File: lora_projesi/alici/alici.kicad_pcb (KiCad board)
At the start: 4 copper layers, 88 x 102 mm, 127 parts, among them J1 USB-C, J2 SMA, J3 RJ45, J4 u.FL (ANA ANTEN), J5 12 V GIRIS, J6 LAMBA, J7 MICRO-SIM, J8 u.FL (YARDIMCI ANTEN, ISTEGE 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, K1 SRD-12VDC-SL-A, Q1 AO3401A, Q2 MMBT2222A, Q3 MMBT2222A, Q4 MMBT2222A, SW1 DUGME, U1 ESP32-S3-WROOM-1-N4, U10 SIM7600SA, U11 AP2112K-3.3, U12 ESDA6V1-5SC6, U4 RFM95W-915S2, U5 TPS62933DRLR, U6 TPS62933DRLR, U7 USBLC6-2SC6, U8 TXB0104PW, U9 W5500, Y1 25 MHz

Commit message: Alici: uretim dosyalari (Gerber, delik, BOM, yerlestirme, PDF)
Co-Authored-By: Claude Sonnet 5.5 <noreply@anthropic.com>
Claude-Session: https://claude.ai/code/session_01Q71gHQtKJ86ZE2CtYTYSwP
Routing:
- net GND: track 232.1 -> 237.4 mm, vias 232 -> 234
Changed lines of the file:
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@@
   (segment (start 35.277707 20.227637) (end 36.177707 20.227637) (width 0.25) (layer "F.Cu") (net 93))
   (segment (start 10.8 91.12) (end 10.8 89.72) (width 0.25) (layer "F.Cu") (net 93))
+  (segment (start 31.15 27.65) (end 31.25 27.75) (width 0.25) (layer "F.Cu") (net 93))
   (segment (start 74.75 90.26) (end 75.65 90.26) (width 0.25) (layer "F.Cu") (net 93))
   (segment (start 37.5 31.9) (end 37.5 32.799999) (width 0.25) (layer "F.Cu") (net 93))
+  (segment (start 31.25 27.75) (end 31.75 27.75) (width 0.25) (layer "F.Cu") (net 93))
   (segment (start 54.75 66.1625) (end 54.75 65.0625) (width 0.25) (layer "F.Cu") (net 93))
+  (segment (start 31.75 27.75) (end 31.8 27.8) (width 0.25) (layer "F.Cu") (net 93))
   (segment (start 51.182401 11.420149) (end 52.082401 11.420149) (width 0.25) (layer "F.Cu") (net 93))
   (segment (start 43.1 37.5) (end 44 37.5) (width 0.25) (layer "F.Cu") (net 93))
@@
   (segment (start 12.9 49.5) (end 13.8 49.5) (width 0.25) (layer "F.Cu") (net 93))
   (segment (start 40.446899 4.070346) (end 41.346899 4.070346) (width 0.25) (layer "F.Cu") (net 93))
+  (segment (start 32.2 28.2) (end 32.2 28.4) (width 0.25) (layer "F.Cu") (net 93))
   (segment (start 50.41465 6.192358) (end 51.051046 6.828754) (width 0.25) (layer "F.Cu") (net 93))
   (segment (start 62.475 11) (end 63.111396 11.636396) (width 0.25) (layer "F.Cu") (net 93))
@@
   (segment (start 46.2125 87) (end 46.848896 87.636396) (width 0.25) (layer "F.Cu") (net 93))
   (segment (start 55.172717 71.925954) (end 56.072717 71.925954) (width 0.25) (layer "F.Cu") (net 93))
+  (segment (start 31.9 27.85) (end 31.9 27.9) (width 0.25) (layer "F.Cu") (net 93))
   (segment (start 37.5 62.1) (end 37.5 61.2) (width 0.25) (layer "F.Cu") (net 93))
   (segment (start 17.2 91.12) (end 19 91.12) (width 0.25) (layer "F.Cu") (net 93))
@@
   (segment (start 44.41465 70.192358) (end 45.31465 70.192358) (width 0.25) (layer "F.Cu") (net 93))
   (segment (start 67.343346 49.686625) (end 68.243346 49.686625) (width 0.25) (layer "F.Cu") (net 93))
+  (segment (start 31.8 27.8) (end 31.85 27.8) (width 0.25) (layer "F.Cu") (net 93))
   (segment (start 21.5 31.9) (end 20.863603 32.536396) (width 0.25) (layer "F.Cu") (net 93))
   (segment (start 58.25 4.5) (end 58.25 5.4) (width 0.25) (layer "F.Cu") (net 93))
   (segment (start 9.581158 35.759225) (end 10.481158 35.759225) (width 0.25) (layer "F.Cu") (net 93))
   (segment (start 42.2125 87) (end 42.848896 87.636396) (width 0.25) (layer "F.Cu") (net 93))
+  (segment (start 31.85 27.8) (end 31.9 27.85) (width 0.25) (layer "F.Cu") (net 93))
   (segment (start 32.85 87.9) (end 33.486396 88.536396) (width 0.25) (layer "F.Cu") (net 93))
   (segment (start 25.1375 28.95) (end 21.441981 30.480733) (width 0.25) (layer "F.Cu") (net 93))
@@
   (segment (start 80.098289 75.215095) (end 80.998289 75.215095) (width 0.25) (layer "F.Cu") (net 93))
   (segment (start 44.090413 64.908678) (end 44.726809 65.545074) (width 0.25) (layer "F.Cu") (net 93))
+  (segment (start 31.9 27.9) (end 32.2 28.2) (width 0.25) (layer "F.Cu") (net 93))
   (segment (start 24.2 28.8) (end 24.25 28.85) (width 0.25) (layer "F.Cu") (net 93))
   (segment (start 67.5 82.54) (end 66.863603 83.176396) (width 0.25) (layer "F.Cu") (net 93))
@@
   (segment (start 12.9 49.5) (end 12 49.5) (width 0.25) (layer "F.Cu") (net 93))
   (segment (start 55.122479 84.448638) (end 55.758875 85.085034) (width 0.25) (layer "F.Cu") (net 93))
+  (segment (start 32.2 28.4) (end 32.65 28.85) (width 0.25) (layer "F.Cu") (net 93))
   (segment (start 36.250064 4.42492) (end 37.150064 4.42492) (width 0.25) (layer "F.Cu") (net 93))
   (segment (start 24.05 28.65) (end 24.1 28.7) (width 0.25) (layer "F.Cu") (net 93))
@@
   (segment (start 35.277707 20.227637) (end 35.914103 20.864033) (width 0.25) (layer "F.Cu") (net 93))
   (segment (start 66.738361 40.358364) (end 67.638361 40.358364) (width 0.25) (layer "F.Cu") (net 93))
+  (segment (start 30.8625 27.65) (end 31.15 27.65) (width 0.25) (layer "F.Cu") (net 93))
   (segment (start 37.5 62.1) (end 38.18883 63.762983) (width 0.25) (layer "F.Cu") (net 93))
   (segment (start 18.5 31.9) (end 18.5 32.799999) (width 0.25) (layer "F.Cu") (net 93))
@@
   (via (at 10.8 89.72) (size 0.5) (drill 0.25) (layers "F.Cu" "B.Cu") (net 93))
   (via (at 34.772645 61.880584) (size 0.5) (drill 0.25) (layers "F.Cu" "B.Cu") (net 93))
+  (via (at 32.65 28.85) (size 0.5) (drill 0.25) (layers "F.Cu" "B.Cu") (net 93))
   (via (at 32.661396 54.256396) (size 0.5) (drill 0.25) (layers "F.Cu" "B.Cu") (net 93))
   (via (at 13.8 45.5) (size 0.5) (drill 0.25) (layers "F.Cu" "B.Cu") (net 93))
@@
   (via (at 38.010756 60.806568) (size 0.5) (drill 0.25) (layers "F.Cu" "B.Cu") (net 93))
   (via (at 34.5 61.2) (size 0.5) (drill 0.25) (layers "F.Cu" "B.Cu") (net 93))
+  (via (at 34.5 31) (size 0.5) (drill 0.25) (layers "F.Cu" "B.Cu") (net 93))
   (via (at 42.721548 66.987703) (size 0.5) (drill 0.25) (layers "F.Cu" "B.Cu") (net 93))
   (via (at 54.834486 79.191631) (size 0.5) (drill 0.25) (layers "F.Cu" "B.Cu") (net 93))
@@
   (segment (start 30.932727 56.971145) (end 30.032727 56.971145) (width 0.25) (layer "B.Cu") (net 93))
   (segment (start 37.475 62.1) (end 38.010756 60.806568) (width 0.25) (layer "B.Cu") (net 93))
+  (segment (start 33.3 29.55) (end 34.45 30.7) (width 0.25) (layer "B.Cu") (net 93))
   (segment (start 33.941154 62.225) (end 34.772645 61.880584) (width 0.25) (layer "B.Cu") (net 93))
   (segment (start 37.475 62.1) (end 37.475 63) (width 0.25) (layer "B.Cu") (net 93))
@@
   (segment (start 30.932727 56.971145) (end 31.832727 56.971145) (width 0.25) (layer "B.Cu") (net 93))
   (segment (start 58.25 4.5) (end 58.886396 5.136396) (width 0.25) (layer "B.Cu") (net 93))
+  (segment (start 33.3 29.5) (end 33.3 29.55) (width 0.25) (layer "B.Cu") (net 93))
   (segment (start 66.75 4.5) (end 67.386396 5.136396) (width 0.25) (layer "B.Cu") (net 93))
   (segment (start 58.25 4.5) (end 57.613603 5.136396) (width 0.25) (layer "B.Cu") (net 93))
+  (segment (start 34.45 30.7) (end 34.45 30.95) (width 0.25) (layer "B.Cu") (net 93))
+  (segment (start 32.65 28.85) (end 33.3 29.5) (width 0.25) (layer "B.Cu") (net 93))
   (segment (start 38.771375 63.976395) (end 39.407771 64.612791) (width 0.25) (layer "B.Cu") (net 93))
   (segment (start 32.025 53.62) (end 32.924999 53.62) (width 0.25) (layer "B.Cu") (net 93))
@@
   (segment (start 28.891013 56.068621) (end 29.791013 56.068621) (width 0.25) (layer "B.Cu") (net 93))
   (segment (start 32.025 53.62) (end 32.661396 54.256396) (width 0.25) (layer "B.Cu") (net 93))
+  (segment (start 34.45 30.95) (end 34.5 31) (width 0.25) (layer "B.Cu") (net 93))
   (segment (start 33.941154 62.225) (end 34.772645 62.569415) (width 0.25) (layer "B.Cu") (net 93))
   (zone (net 93) (net_name "GND") (layer "In1.Cu") (hatch edge 0.5)

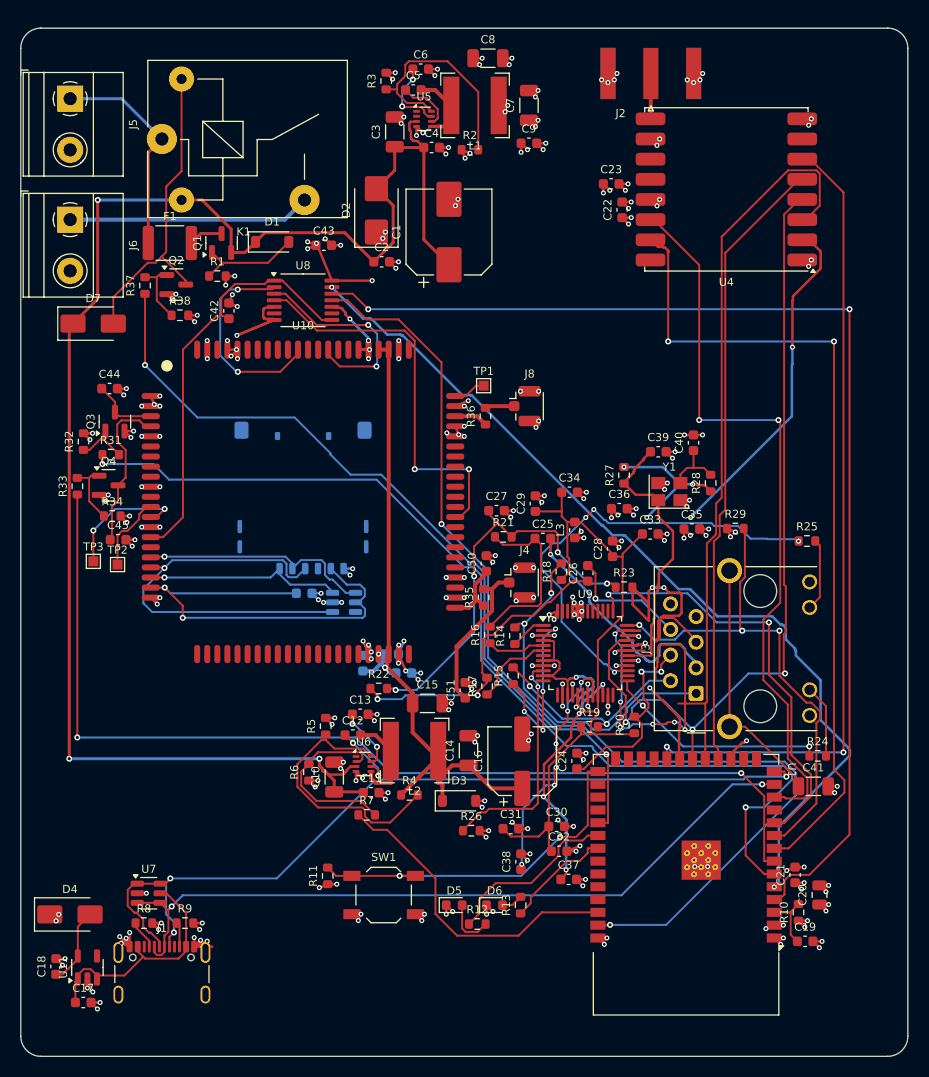
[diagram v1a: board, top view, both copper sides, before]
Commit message: Alici: guc izleri genisletiliyor (ara hal)
Co-Authored-By: Claude Sonnet 5.5 <noreply@anthropic.com>
Claude-Session: https://claude.ai/code/session_01Q71gHQtKJ86ZE2CtYTYSwP
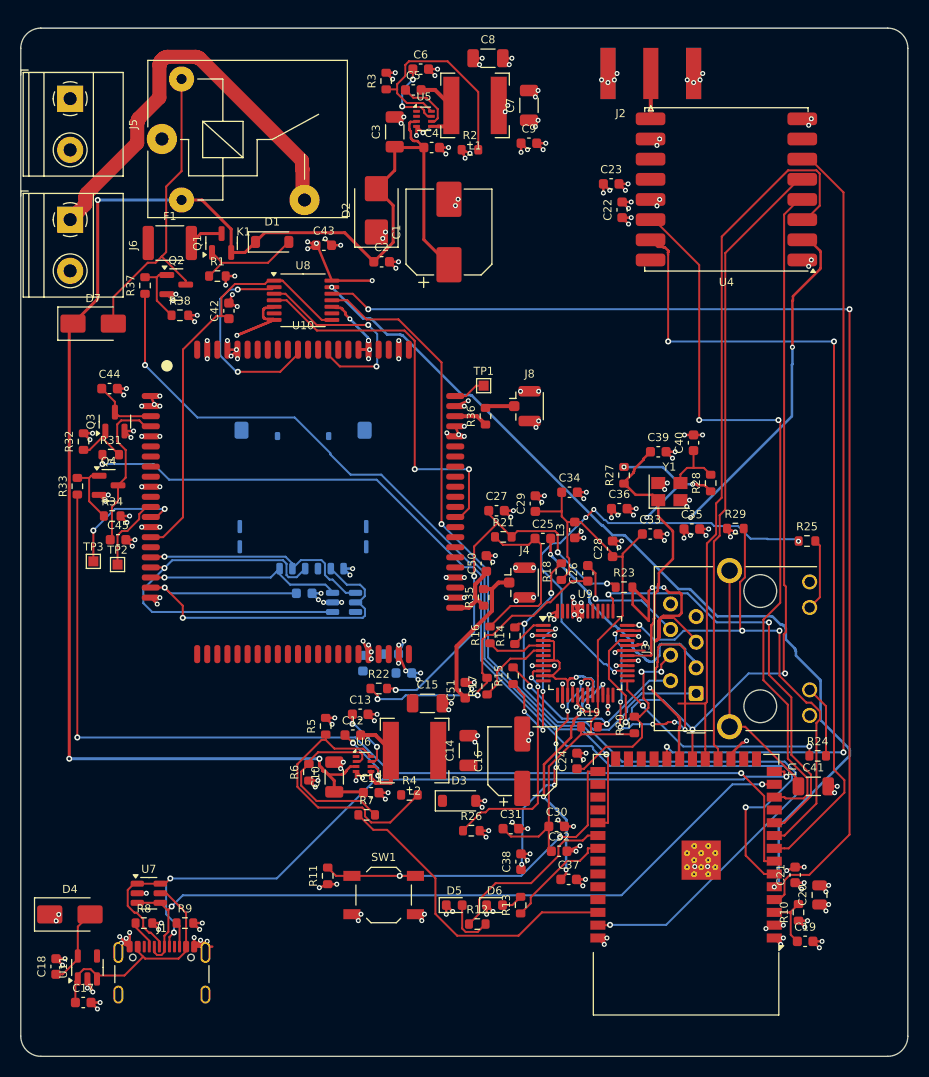
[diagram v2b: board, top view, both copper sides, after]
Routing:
- net VBAT_MOD: track 69.6 -> 0.00 mm, vias 2 -> 0
- net +12V_IN: track 21.6 -> 0.00 mm
- net LAMBA_SW: track 24.1 -> 41.9 mm
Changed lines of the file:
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@@
   (segment (start 17.8593 20.3824) (end 16.9218 21.3199) (width 0.3) (layer "F.Cu") (net 6))
   (segment (start 19.9218 20.3824) (end 17.8593 20.3824) (width 0.3) (layer "F.Cu") (net 6))
-  (segment (start 12.6468 21.3199) (end 12.6468 12.3532) (width 0.3) (layer "F.Cu") (net 7))
-  (segment (start 12.6468 12.3532) (end 14 11) (width 0.3) (layer "F.Cu") (net 7))
-  (segment (start 4.9 7) (end 10 7) (width 0.3) (layer "B.Cu") (net 7))
-  (segment (start 10 7) (end 14 11) (width 0.3) (layer "B.Cu") (net 7))
   (segment (start 54.85 69.05) (end 54.85 68.7) (width 0.25) (layer "F.Cu") (net 8))
   (segment (start 51.9 76.2) (end 51.9 73.05) (width 0.25) (layer "F.Cu") (net 8))
@@
   (segment (start 24.5201 23.2827) (end 26.5899 21.2129) (width 0.2) (layer "F.Cu") (net 26))
   (segment (start 19.85 23.4281) (end 18.6809 24.5972) (width 0.2) (layer "F.Cu") (net 26))
-  (segment (start 26.2 19) (end 28.15 17.05) (width 0.4) (layer "B.Cu") (net 27))
-  (segment (start 4.9 19) (end 26.2 19) (width 0.4) (layer "B.Cu") (net 27))
+  (segment (start 4.9 19) (end 6.4 17.5) (width 1.4) (layer "F.Cu") (net 27))
+  (segment (start 6.5 16.5) (end 6.55 16.45) (width 1.4) (layer "F.Cu") (net 27))
+  (segment (start 13.8 3.6) (end 13.8 3.45) (width 1.4) (layer "F.Cu") (net 27))
+  (segment (start 11.65 9.05) (end 11.7 9) (width 1.4) (layer "F.Cu") (net 27))
+  (segment (start 13.9 3.3) (end 13.9 3.25) (width 1.4) (layer "F.Cu") (net 27))
+  (segment (start 27.95 14) (end 27.95 16.85) (width 1.4) (layer "F.Cu") (net 27))
+  (segment (start 6.45 16.6) (end 6.5 16.55) (width 1.4) (layer "F.Cu") (net 27))
+  (segment (start 6.4 17.5) (end 6.4 16.8) (width 1.4) (layer "F.Cu") (net 27))
+  (segment (start 11.7 8.95) (end 13.75 6.9) (width 1.4) (layer "F.Cu") (net 27))
+  (segment (start 11.55 9.35) (end 11.6 9.3) (width 1.4) (layer "F.Cu") (net 27))
+  (segment (start 11.6 9.15) (end 11.65 9.1) (width 1.4) (layer "F.Cu") (net 27))
+  (segment (start 17.4 2.9) (end 17.55 2.9) (width 1.4) (layer "F.Cu") (net 27))
+  (segment (start 27.9 13.15) (end 27.9 13.95) (width 1.4) (layer "F.Cu") (net 27))
+  (segment (start 17.55 2.9) (end 17.6 2.95) (width 1.4) (layer "F.Cu") (net 27))
+  (segment (start 14.25 2.95) (end 14.3 2.95) (width 1.4) (layer "F.Cu") (net 27))
+  (segment (start 6.5 16.55) (end 6.5 16.5) (width 1.4) (layer "F.Cu") (net 27))
+  (segment (start 17.35 2.85) (end 17.4 2.9) (width 1.4) (layer "F.Cu") (net 27))
+  (segment (start 14.35 2.9) (end 14.5 2.9) (width 1.4) (layer "F.Cu") (net 27))
+  (segment (start 17.7 3) (end 17.75 3) (width 1.4) (layer "F.Cu") (net 27))
+  (segment (start 6.55 16.45) (end 6.55 16.4) (width 1.4) (layer "F.Cu") (net 27))
+  (segment (start 11.7 9) (end 11.7 8.95) (width 1.4) (layer "F.Cu") (net 27))
+  (segment (start 17.65 2.95) (end 17.7 3) (width 1.4) (layer "F.Cu") (net 27))
+  (segment (start 11.55 11.4) (end 11.55 9.35) (width 1.4) (layer "F.Cu") (net 27))
+  (segment (start 11.6 9.3) (end 11.6 9.15) (width 1.4) (layer "F.Cu") (net 27))
+  (segment (start 6.55 16.4) (end 11.55 11.4) (width 1.4) (layer "F.Cu") (net 27))
+  (segment (start 13.85 3.4) (end 13.85 3.35) (width 1.4) (layer "F.Cu") (net 27))
+  (segment (start 14.3 2.95) (end 14.35 2.9) (width 1.4) (layer "F.Cu") (net 27))
+  (segment (start 14.15 3) (end 14.2 3) (width 1.4) (layer "F.Cu") (net 27))
+  (segment (start 14.55 2.85) (end 17.35 2.85) (width 1.4) (layer "F.Cu") (net 27))
+  (segment (start 17.6 2.95) (end 17.65 2.95) (width 1.4) (layer "F.Cu") (net 27))
+  (segment (start 6.45 16.75) (end 6.45 16.6) (width 1.4) (layer "F.Cu") (net 27))
+  (segment (start 11.65 9.1) (end 11.65 9.05) (width 1.4) (layer "F.Cu") (net 27))
+  (segment (start 27.9 13.95) (end 27.95 14) (width 1.4) (layer "F.Cu") (net 27))
+  (segment (start 17.75 3) (end 27.9 13.15) (width 1.4) (layer "F.Cu") (net 27))
+  (segment (start 27.95 16.85) (end 28.15 17.05) (width 1.4) (layer "F.Cu") (net 27))
+  (segment (start 13.75 6.9) (end 13.75 3.65) (width 1.4) (layer "F.Cu") (net 27))
+  (segment (start 13.9 3.25) (end 14.15 3) (width 1.4) (layer "F.Cu") (net 27))
+  (segment (start 13.8 3.45) (end 13.85 3.4) (width 1.4) (layer "F.Cu") (net 27))
+  (segment (start 14.5 2.9) (end 14.55 2.85) (width 1.4) (layer "F.Cu") (net 27))
+  (segment (start 6.4 16.8) (end 6.45 16.75) (width 1.4) (layer "F.Cu") (net 27))
+  (segment (start 13.85 3.35) (end 13.9 3.3) (width 1.4) (layer "F.Cu") (net 27))
+  (segment (start 14.2 3) (end 14.25 2.95) (width 1.4) (layer "F.Cu") (net 27))
+  (segment (start 13.75 3.65) (end 13.8 3.6) (width 1.4) (layer "F.Cu") (net 27))
   (segment (start 45.3267 89.6586) (end 44.125 89.6586) (width 0.2) (layer "F.Cu") (net 28))
   (segment (start 44.125 89.6586) (end 43.7875 89.3211) (width 0.2) (layer "F.Cu") (net 28))
@@
   (segment (start 34.1277 55.6835) (end 33.6534 55.2092) (width 0.2) (layer "B.Cu") (net 81))
   (segment (start 34.1463 57.6064) (end 34.1463 58.283) (width 0.2) (layer "B.Cu") (net 81))
-  (segment (start 36.3792 62.2208) (end 36.4195 62.1805) (width 0.4) (layer "F.Cu") (net 82))
-  (segment (start 36.3389 62.2794) (end 36.3389 62.2702) (width 0.4) (layer "F.Cu") (net 82))
-  (segment (start 36.3389 62.4078) (end 36.3389 62.3344) (width 0.4) (layer "F.Cu") (net 82))
-  (segment (start 46.6925 75.4202) (end 49.7484 75.4202) (width 0.4) (layer "F.Cu") (net 82))
-  (segment (start 36.4195 62.1805) (end 36.5 62.1) (width 0.4) (layer "F.Cu") (net 82))
-  (segment (start 36.3591 62.2409) (end 36.3792 62.2208) (width 0.4) (layer "F.Cu") (net 82))
-  (segment (start 36.3389 63.4349) (end 36.1352 63.4349) (width 0.4) (layer "F.Cu") (net 82))
-  (segment (start 36.3389 62.2656) (end 36.3389 62.2633) (width 0.4) (layer "F.Cu") (net 82))
-  (segment (start 35.5 31.9) (end 36.5 31.9) (width 0.4) (layer "F.Cu") (net 82))
-  (segment (start 36.3389 62.2613) (end 36.3389 62.2612) (width 0.4) (layer "F.Cu") (net 82))
-  (segment (start 36.3389 62.2702) (end 36.3389 62.2656) (width 0.4) (layer "F.Cu") (net 82))
-  (segment (start 36.3389 62.2622) (end 36.3389 62.2616) (width 0.4) (layer "F.Cu") (net 82))
-  (segment (start 38.8715 66.9877) (end 38.8715 65.9675) (width 0.4) (layer "F.Cu") (net 82))
-  (segment (start 36.3389 62.2612) (end 36.3389 62.2611) (width 0.4) (layer "F.Cu") (net 82))
-  (segment (start 41.6229 74.3172) (end 42.7977 73.1424) (width 0.4) (layer "F.Cu") (net 82))
-  (segment (start 36.344 62.256) (end 36.349 62.251) (width 0.4) (layer "F.Cu") (net 82))
-  (segment (start 38.8715 65.9675) (end 36.3389 63.4349) (width 0.4) (layer "F.Cu") (net 82))
-  (segment (start 36.3389 62.2977) (end 36.3389 62.2794) (width 0.4) (layer "F.Cu") (net 82))
-  (segment (start 40.6719 73.1299) (end 37.7334 76.0684) (width 0.4) (layer "F.Cu") (net 82))
-  (segment (start 42.7977 73.1424) (end 44.4147 73.1424) (width 0.4) (layer "F.Cu") (net 82))
-  (segment (start 38.8715 69.8554) (end 41.4147 72.3986) (width 0.4) (layer "F.Cu") (net 82))
-  (segment (start 36.3389 62.848) (end 36.3389 62.5545) (width 0.4) (layer "F.Cu") (net 82))
-  (segment (start 36.3389 62.3344) (end 36.3389 62.2977) (width 0.4) (layer "F.Cu") (net 82))
-  (segment (start 36.3389 62.2633) (end 36.3389 62.2622) (width 0.4) (layer "F.Cu") (net 82))
-  (segment (start 36.3389 62.2616) (end 36.3389 62.2613) (width 0.4) (layer "F.Cu") (net 82))
-  (segment (start 38.8715 66.9877) (end 38.8715 69.8554) (width 0.4) (layer "F.Cu") (net 82))
-  (segment (start 36.349 62.251) (end 36.3591 62.2409) (width 0.4) (layer "F.Cu") (net 82))
-  (segment (start 36.3389 63.4349) (end 36.3389 62.848) (width 0.4) (layer "F.Cu") (net 82))
-  (segment (start 44.4147 73.1424) (end 46.6925 75.4202) (width 0.4) (layer "F.Cu") (net 82))
-  (segment (start 41.4147 74.8691) (end 41.6229 74.8691) (width 0.4) (layer "F.Cu") (net 82))
-  (segment (start 41.8311 75.0773) (end 41.6229 74.8691) (width 0.4) (layer "F.Cu") (net 82))
-  (segment (start 41.4147 72.3986) (end 41.4147 73.1299) (width 0.4) (layer "F.Cu") (net 82))
-  (segment (start 36.3389 62.2611) (end 36.344 62.256) (width 0.4) (layer "F.Cu") (net 82))
-  (segment (start 41.8311 76.6563) (end 41.8311 75.0773) (width 0.4) (layer "F.Cu") (net 82))
-  (segment (start 41.4147 73.1299) (end 40.6719 73.1299) (width 0.4) (layer "F.Cu") (net 82))
-  (segment (start 41.6229 74.8691) (end 41.6229 74.3172) (width 0.4) (layer "F.Cu") (net 82))
-  (segment (start 36.5 31.9) (end 36.5 62.1) (width 0.4) (layer "F.Cu") (net 82))
-  (segment (start 41.4147 71.6674) (end 41.4147 72.3986) (width 0.4) (layer "F.Cu") (net 82))
-  (segment (start 41.4147 73.1299) (end 41.4147 74.8691) (width 0.4) (layer "F.Cu") (net 82))
-  (segment (start 36.3389 62.5545) (end 36.3389 62.4078) (width 0.4) (layer "F.Cu") (net 82))
-  (via (at 36.1352 63.4349) (size 0.6) (drill 0.3) (layers "F.Cu" "B.Cu") (net 82))
-  (via (at 35.5 62.1) (size 0.5) (drill 0.25) (layers "F.Cu" "B.Cu") (net 82))
-  (segment (start 37.2214 63.9764) (end 36.6767 63.9764) (width 0.4) (layer "B.Cu") (net 82))
-  (segment (start 35.9 62.1) (end 35.5 62.1) (width 0.4) (layer "B.Cu") (net 82))
-  (segment (start 34.9847 63.775) (end 33.9412 63.775) (width 0.4) (layer "B.Cu") (net 82))
-  (segment (start 35.925 62.8347) (end 35.73 63.0297) (width 0.4) (layer "B.Cu") (net 82))
-  (segment (start 36.1352 63.4349) (end 35.73 63.0297) (width 0.4) (layer "B.Cu") (net 82))
-  (segment (start 36.6767 63.9764) (end 36.1352 63.4349) (width 0.4) (layer "B.Cu") (net 82))
-  (segment (start 35.925 62.1) (end 35.925 62.8347) (width 0.4) (layer "B.Cu") (net 82))
-  (segment (start 35.73 63.0297) (end 34.9847 63.775) (width 0.4) (layer "B.Cu") (net 82))
   (segment (start 14.4433 85.8238) (end 13.834 85.8238) (width 0.2) (layer "F.Cu") (net 83))
   (segment (start 6.9326 93.3547) (end 6.2395 93.3547) (width 0.2) (layer "F.Cu") (net 83))
